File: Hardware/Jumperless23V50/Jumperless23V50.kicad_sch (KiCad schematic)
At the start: 218 parts, among them J1 Debug, J11 TopOutMAIN, J12 TopInMAIN, J13 BottomInMAIN, J14 5V, J15 BottomOutMAIN, J1711 Conn_01x15, J1712 Conn_01x15, J2 USB_C_Receptacle_USB2.0_16P, J3 ProbeJack, J4 Breadboard, J5 ProbeHeader, J6 CH446Q, J7 DaisyChain_OUT, J8 DaisyChain_IN, K1 CH446Q, Q3 Q_NPN_CBE, SW1 BOOT, SW3 RotaryEncoder_Switch, U1 LT1054, U10 L272D, U11 LM324, U1806 MCP4728, U1807 L272D, U2 NCP1117-3.3_SOT223, U3 INA219, U4 INA219, U5 RP2350_80QFN, U7 LM324, U8 W25Q128JVS, U9 RP2040, Y1 ABLS-12.000MHZ-B4-T

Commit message: Fixed lockups - added Apps to Menu - routed 23V50
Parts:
- removed C12: 1uF, Capacitor_SMD:C_0402_1005Metric, symbol JumperlessSymbols:C
- removed D63, D66: 1N4148, Diode_SMD:D_SOD-323, symbol JumperlessSymbols:1N4148W
- removed J5: ProbeHeader, JumperlessFootprints:probePads, symbol Connector_Generic:Conn_01x05
- removed R11, R83, R84, R9: 0R, Resistor_SMD:R_0402_1005Metric, symbol JumperlessSymbols:R_Small_US_2
- removed R2, R3: 22R, Resistor_SMD:R_0402_1005Metric, symbol JumperlessSymbols:R
- removed unit 4 of RN15
- removed unit 3 of RN15
- removed RN5: 0R, Resistor_SMD:R_Array_Convex_4x0402, symbol Device:R_Pack04_Split
- removed TP13: -8V, JumperlessFootprints:TestPoint_D0.75mm, symbol JumperlessSymbols:TestPoint
- removed TP14: +8V, JumperlessFootprints:TestPoint_D0.75mm, symbol JumperlessSymbols:TestPoint
- removed TP15: LED IN_FROM_WISHBONE, JumperlessFootprints:PINHEADER-1x1_vertical, symbol JumperlessSymbols:TestPoint
- removed TP2: TestPoint, JumperlessFootprints:TestPoint_Pad_D1.0mm, symbol Connector:TestPoint
- removed TP21: DAC_1, JumperlessFootprints:TestPoint_D0.75mm, symbol JumperlessSymbols:TestPoint
- removed U9: RP2040, JumperlessFootprints:RP2040-QFN-56, symbol JumperlessSymbols:RP2040
- added JP10: Nano GND Top - GPIO 24, JumperlessFootprints:SolderJumper-3_P1.3mm_Bridged12_Pad1.0x1.5mm, symbol JumperlessSymbols:SolderJumper_3_Bridged12
- added JP12: Nano GND Bot - GPIO 23, JumperlessFootprints:SolderJumper-3_P1.3mm_Bridged12_Pad1.0x1.5mm, symbol JumperlessSymbols:SolderJumper_3_Bridged12
- added JP13: GND, JumperlessFootprints:SolderJumper_2_Bridged_Small, symbol JumperlessSymbols:SolderJumper_2_Bridged
- added JP14: ADC, JumperlessFootprints:SolderJumper_2_Bridged_Small, symbol JumperlessSymbols:SolderJumper_2_Bridged
- added JP15: GP2, JumperlessFootprints:SolderJumper_2_Bridged_Small, symbol JumperlessSymbols:SolderJumper_2_Bridged
- added JP16: BUT, JumperlessFootprints:SolderJumper_2_Bridged_Small, symbol JumperlessSymbols:SolderJumper_2_Bridged
- added JP17: PRO, JumperlessFootprints:SolderJumper_2_Bridged_Small, symbol JumperlessSymbols:SolderJumper_2_Bridged
- added JP5: Reset 0 - Current Sense +, JumperlessFootprints:SolderJumper-3_P1.3mm_Bridged12_Pad1.0x1.5mm, symbol JumperlessSymbols:SolderJumper_3_Bridged12
- added JP6: Reset 1 - Current Sense -, JumperlessFootprints:SolderJumper-3_P1.3mm_Bridged12_Pad1.0x1.5mm, symbol JumperlessSymbols:SolderJumper_3_Bridged12
- added JP7: Reset 0, JumperlessFootprints:SolderJumper_2_Bridged_Small, symbol JumperlessSymbols:SolderJumper_2_Bridged
- added JP8: Reset 1, JumperlessFootprints:SolderJumper_2_Bridged_Small, symbol JumperlessSymbols:SolderJumper_2_Bridged
- added JP9: VIN - GPIO 25, JumperlessFootprints:SolderJumper-3_P1.3mm_Bridged12_Pad1.0x1.5mm, symbol JumperlessSymbols:SolderJumper_3_Bridged12
- added R2, R80, R89, R90: 0R, Resistor_SMD:R_0402_1005Metric_Pad0.72x0.64mm_HandSolder, symbol Device:R_Small_US
- added TP2: RUN, JumperlessFootprints:TestPoint_D0.75mm, symbol JumperlessSymbols:TestPoint
- added U12: ~, JumperlessFootprints:SolderJumper-Double, symbol JumperlessSymbols:SolderJumperDouble
- added U6: TLV73311PDBV, Package_TO_SOT_SMD:SOT-23-5, symbol Regulator_Linear:TLV73311PDBV
- added U9: LM2660MX, JumperlessFootprints:SOIC8, symbol Converter_DCDC:TC7662Bx0A
- A2, B1, C26, E1, F5, G1, H1, I1, K1, L1: LCSC (none) -> C109471; LCSC Part # (none) -> C109471
- C1, C4, C6: footprint Capacitor_SMD:C_1206_3216Metric_Pad1.33x1.80mm_HandSolder -> JumperlessFootprints:1210CAP; LCSC (none) -> C6120014
- C11, C9: value 1uF -> 10uF; footprint Capacitor_SMD:C_0402_1005Metric -> Capacitor_SMD:C_0603_1608Metric
- C16, C25: footprint RP2350_80QFN_minimal:C_0402_1005Metric_small_pads -> JumperlessFootprints:C_0402_1005Metric
- C2, C3, C5: value 10uF -> 22uF; footprint Capacitor_Tantalum_SMD:CP_EIA-3528-12_Kemet-T_Pad1.50x2.35mm_HandSolder -> JumperlessFootprints:1210CAP; LCSC C189401 -> C212712; LCSC Part # (none) -> C212712
- C27: value 0.1uF -> .1uF
- D61, D62, D65, D67, D68: footprint Diode_SMD:D_SOD-323 -> JumperlessFootprints:D_SOD-323; LCSC (none) -> C150183; LCSC Part # (none) -> C150183
- JP1: value NANO 3V3 -> NANO 3V3 - GPIO 27; footprint JumperlessFootprints:SolderJumper_2_Bridged_Small -> JumperlessFootprints:SolderJumper-3_P1.3mm_Bridged12_Pad1.0x1.5mm; symbol JumperlessSymbols:SolderJumper_2_Bridged -> JumperlessSymbols:SolderJumper_3_Bridged12; now left out of the parts list
- JP11: footprint Jumper:SolderJumper-3_P1.3mm_Bridged12_Pad1.0x1.5mm -> JumperlessFootprints:SolderJumper-3_P1.3mm_Bridged12_Pad1.0x1.5mm
- JP2: value NANO 5V -> NANO 5V - GPIO 26; footprint JumperlessFootprints:SolderJumper_2_Bridged_Small -> JumperlessFootprints:SolderJumper-3_P1.3mm_Bridged12_Pad1.0x1.5mm; symbol JumperlessSymbols:SolderJumper_2_Bridged -> JumperlessSymbols:SolderJumper_3_Bridged12; now left out of the parts list
- L2: LCSC (none) -> C2041573; LCSC Part # (none) -> C2041573
- Q3: value Q_NPN_CBE -> Q_NPN_BCE; footprint (none) -> Package_TO_SOT_SMD:SOT-23; symbol Device:Q_NPN_CBE -> Device:Q_NPN_BEC; LCSC (none) -> C909754; LCSC Part # (none) -> C909754
- R21, R55, R56, R58, R59, R60, R61, R62, R63, R64, R65, R66, R67, R68, R69, R70, R71, R72, R73, R74, R75, R76, R77, R78: LCSC C114765 -> C427231; LCSC Part # C114765 -> C427231
- R31: LCSC (none) -> C852887
- R6: LCSC (none) -> C852624; LCSC Part # (none) -> C852624
- R7, R88: LCSC (none) -> C131359; LCSC Part # (none) -> C131359
- R79: LCSC (none) -> C427231; LCSC Part # (none) -> C427231
- R8: value 47K -> 51100; LCSC (none) -> C852827; LCSC Part # (none) -> C852827
- R85, R86: LCSC C114765 -> C852651; LCSC Part # C114765 -> C852651
- RN10, RN19: LCSC C621323 -> C728748; LCSC Part # C621323 -> C728748
- RN12: value 10K -> 8.2K; LCSC C136853 -> C728757; LCSC Part # C136853 -> C728757
- RN13, RN16, RN7: value 6.8K -> 8.2K; LCSC C728919 -> C728757; LCSC Part # C728919 -> C728757
- RN14, RN17, RN6: LCSC C2769517 -> C620895; LCSC Part # C2769517 -> C620895
- RN15, RN18: LCSC C621323 -> C425315; LCSC Part # C621323 -> C425315
- RN15: renamed from RN11; LCSC C621323 -> C425315; LCSC Part # C621323 -> C425315
- RN18: renamed from RN15; LCSC C621323 -> C425315; LCSC Part # C621323 -> C425315
- RN2, RN3: LCSC (none) -> C425316; LCSC Part # (none) -> C425316
- RN4, RN8: LCSC C2769517 -> C2769517; LCSC Part # C2769517 -> C2769517
- SW1: LCSC (none) -> C22459525; LCSC Part # (none) -> C22459525
- SW3: LCSC (none) -> C29780879; LCSC Part # (none) -> C29780879
- TP22, TP23: footprint Symbol:BackMaskWindows -> JumperlessFootprints:backMaskWindowsNew
- TP5: value FB/SHDN -> +9V
- TP6: value VREF -> -9V
- U1: footprint JumperlessFootprints:DIP-8_W7.62mm -> JumperlessFootprints:DIP8; LCSC (none) -> C1355744; LCSC Part # (none) -> C1355744; now not fitted; now left out of the parts list
- U10, U1807: LCSC (none) -> C443843; LCSC Part # (none) -> C443843
- U11, U7: LCSC (none) -> C71035; LCSC Part # (none) -> C71035
- U1806: LCSC (none) -> C108207; LCSC Part # (none) -> C108207
- U2: LCSC (none) -> C22462596; LCSC Part # (none) -> C22462596
- U3, U4: footprint Package_SO:SOIC-8_3.9x4.9mm_P1.27mm -> JumperlessFootprints:SOIC8; LCSC (none) -> C138706; LCSC Part # (none) -> C138706
- U8: LCSC (none) -> C97521; LCSC Part # (none) -> C97521
- Y1: value ABLS-12.000MHZ-B4-T -> ABM8-272-T3; LCSC (none) -> C20625731; LCSC Part # (none) -> C20625731
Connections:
- net +1V1: now also R80.1, R89.2; no longer C11.1, C9.1, U5.65 (VREG_FB)
- net +5V: now also C11.1, C9.1, R2.1, U6.1 (IN), U6.3 (EN), U9.8 (V+)
- net +9V: now also TP5.1
- net -9V: now also TP6.1
- net 1: now also A2.35 (Y1); no longer K1.31 (X0)
- net 10: now also B1.39 (Y3); no longer B1.37 (Y2)
- net 11: now also B1.17 (Y4); no longer B1.39 (Y3)
- net 12: now also B1.15 (Y5); no longer B1.17 (Y4)
- net 13: now also B1.13 (Y6); no longer B1.15 (Y5)
- net 14: now also B1.11 (Y7); no longer B1.13 (Y6)
- net 15: now also C26.35 (Y1); no longer B1.11 (Y7)
- net 16: now also C26.37 (Y2); no longer C26.35 (Y1)
- net 17: now also C26.39 (Y3); no longer C26.37 (Y2)
- net 18: now also C26.17 (Y4); no longer C26.39 (Y3)
- net 19: now also C26.15 (Y5); no longer C26.17 (Y4)
- net 2: now also A2.37 (Y2); no longer A2.35 (Y1)
- net 20: now also C26.13 (Y6); no longer C26.15 (Y5)
- net 21: now also C26.11 (Y7); no longer C26.13 (Y6)
- net 22: now also D70.35 (Y1); no longer C26.11 (Y7)
- net 23: now also D70.37 (Y2); no longer D70.35 (Y1)
- net 24: now also D70.39 (Y3); no longer D70.37 (Y2)
- net 25: now also D70.17 (Y4); no longer D70.39 (Y3)
- net 26: now also D70.15 (Y5); no longer D70.17 (Y4)
- net 27: now also D70.13 (Y6); no longer D70.15 (Y5)
- net 28: now also D70.11 (Y7); no longer D70.13 (Y6)
- net 29: now also K1.31 (X0); no longer D70.11 (Y7)
- net 3: now also A2.39 (Y3); no longer A2.37 (Y2)
- net 30: now also L1.31 (X0); no longer K1.30 (X1)
- net 31: now also E1.35 (Y1); no longer L1.31 (X0)
- net 32: now also E1.37 (Y2); no longer E1.35 (Y1)
- net 33: now also E1.39 (Y3); no longer E1.37 (Y2)
- net 34: now also E1.17 (Y4); no longer E1.39 (Y3)
- net 35: now also E1.15 (Y5); no longer E1.17 (Y4)
- net 36: now also E1.13 (Y6); no longer E1.15 (Y5)
- net 37: now also E1.11 (Y7); no longer E1.13 (Y6)
- net 38: now also F5.35 (Y1); no longer E1.11 (Y7)
- net 39: now also F5.37 (Y2); no longer F5.35 (Y1)
- net 4: now also A2.17 (Y4); no longer A2.39 (Y3)
- net 40: now also F5.39 (Y3); no longer F5.37 (Y2)
- net 41: now also F5.17 (Y4); no longer F5.39 (Y3)
- net 42: now also F5.15 (Y5); no longer F5.17 (Y4)
- net 43: now also F5.13 (Y6); no longer F5.15 (Y5)
- net 44: now also F5.11 (Y7); no longer F5.13 (Y6)
- net 45: now also G1.35 (Y1); no longer F5.11 (Y7)
- net 46: now also G1.37 (Y2); no longer G1.35 (Y1)
- net 47: now also G1.39 (Y3); no longer G1.37 (Y2)
- net 48: now also G1.17 (Y4); no longer G1.39 (Y3)
- net 49: now also G1.15 (Y5); no longer G1.17 (Y4)
- net 5: now also A2.15 (Y5); no longer A2.17 (Y4)
- net 50: now also G1.13 (Y6); no longer G1.15 (Y5)
- net 51: now also G1.11 (Y7); no longer G1.13 (Y6)
- net 52: now also H1.35 (Y1); no longer G1.11 (Y7)
- net 53: now also H1.37 (Y2); no longer H1.35 (Y1)
- net 54: now also H1.39 (Y3); no longer H1.37 (Y2)
- net 55: now also H1.17 (Y4); no longer H1.39 (Y3)
- net 56: now also H1.15 (Y5); no longer H1.17 (Y4)
- net 57: now also H1.13 (Y6); no longer H1.15 (Y5)
- net 58: now also H1.11 (Y7); no longer H1.13 (Y6)
- net 59: now also K1.30 (X1); no longer H1.11 (Y7)
- net 6: now also A2.13 (Y6); no longer A2.15 (Y5)
- net 7: now also A2.11 (Y7); no longer A2.13 (Y6)
- net 8: now also B1.35 (Y1); no longer A2.11 (Y7)
- net 9: now also B1.37 (Y2); no longer B1.35 (Y1)
- net ADC_UNBUFFERED_+-8V_PROBE: now also JP14.1 (A); no longer J3.5 (R3)
- net CURR_SENSE+: now also JP5.1 (A), U12.4 (B); no longer I1.8 (X11)
- net CURR_SENSE-: now also JP6.1 (A), U12.5 (B); no longer J6.8 (X11)
- net DAC_1: now also U12.2 (A), U12.6 (C); no longer C10.1, RN8.5 (R4.2), TP8.1, U10.5
- net GND: now also JP10.1 (A), JP12.1 (A), JP13.1 (A), U6.2 (GND), U9.3 (GND); no longer A1.29 (GND), A1.4 (GND), J3.1 (S)
- net GPIO_2: now also JP15.1 (A); no longer J3.4 (R2)
- net GPIO_23: now also JP12.3 (B)
- net GPIO_24: now also JP10.3 (B)
- net GPIO_25: now also JP9.3 (B)
- net GPIO_26: now also JP2.3 (B)
- net GPIO_27: now also JP1.3 (B)
- net NANO_~{RESET}_0: now also JP5.3 (B), JP7.1 (A); no longer U5.18 (GPIO18)
- net NANO_~{RESET}_1: now also JP6.3 (B), JP8.1 (A); no longer U5.19 (GPIO19)
- net Probe_Button: now also JP16.1 (A); no longer J3.3 (R1)
- net Probe_Probe: now also JP17.1 (A); no longer J3.2 (T)
- net RUN: now also TP2.1
- net UART_Rx: now also U5.78 (GPIO1)
- net UART_Tx: now also U5.77 (GPIO0)
- net VIN: now also JP9.1 (A); no longer A1.30 (VIN)
- net VREG_LX: now also R90.2; no longer L2.2
- net Vout: now reaches C4.2, R7.1, U1.5 (-VOUT)
- net Vout: now also Q3.2 (E), U9.5 (VOUT); no longer Q3.3 (E)
- net at D65.1 (K), R7.2: now also Q3.3 (C); no longer Q3.1 (C)
- net at R6.1: now also Q3.1 (B); no longer Q3.2 (B)
- net VREF/LV: now reaches U1.6 (VREF)
- net VREF/LV: now also U9.6 (LV); no longer TP6.1
- net Cap+: now reaches C2.2, C3.1, U1.2 (CAP+)
- net Cap+: now also U9.2 (CAP+)
- net Cap-: now reaches C3.2, C5.1, U1.4 (CAP-)
- net Cap-: now also U9.4 (CAP-)
- net FP/Boost: now reaches U1.1 (FB/SHDN)
- net FP/Boost: now also R2.2, U9.1 (BOOST); no longer TP5.1
- net OSC: now reaches U1.7 (OSC)
- net OSC: now also U9.7 (OSC)
- new net: J3.1 (S), JP13.2 (B)
- new net: J3.2 (T), JP17.2 (B)
- new net: J3.3 (R1), JP16.2 (B)
- new net: J3.4 (R2), JP15.2 (B)
- new net: J3.5 (R3), JP14.2 (B)
- new net: A1.4 (GND), JP10.2 (C)
- new net: R89.1, U6.5 (OUT)
- new net: A1.30 (VIN), JP9.2 (C)
- new net: C10.1, RN8.5 (R4.2), TP8.1, U10.5, U12.3 (C)
- new net: A1.29 (GND), JP12.2 (C)
- new net: JP7.2 (B), U5.18 (GPIO18)
- new net: JP8.2 (B), U5.19 (GPIO19)
- new net: R80.2, U5.65 (VREG_FB)
- new net: J6.8 (X11), JP6.2 (C)
- new net: I1.8 (X11), JP5.2 (C)
- new net: L2.2, R90.1
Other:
- note added: "If we trade routable Nano Resets for Current Sense, we can cut these so they're +-9V tolerant"
- note added: "If you trade routable Nano Resets for Current Sensing, you can hook it up to read DAC 1 current to measure resistance (like DAC 0)"
- note added: "If you want to use a board with a completely different footprint, you can cut and swap all these solder jumpers so they're routable as GPIO 23-27"
- note added: "Rx and Tx relative to the RP2350"
- note added: "So I can swap over to the LDO if this SMPS is being a dick"
- note added: "This is just to make it easy to swap things if I fuck something up"
- note added: "This is to help it not fail startup when Vout goes above any other pin (weird)"
- note removed: "Drop supply voltage by 1 or 2 diode drops so crosspoints don't see voltages too near their supply voltage"
- note removed: "Rx and Tx are relative to the RP2040"
- note removed: "Try the LDO too"
- moved on the sheet: A2, B1, C1, C2, C26, C3, C4, C5, C6, D61, D62, D65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

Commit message: add updates
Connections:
- net +5V: no longer U1.8 (V+)
- net Cap+: no longer U1.2 (CAP+)
- net Cap-: no longer U1.4 (CAP-)
- net FP/Boost: no longer U1.1 (FB/SHDN)
- net GND: no longer U1.3 (GND)
- net OSC: no longer U1.7 (OSC)
- net VREF/LV: no longer U1.6 (VREF)
- net Vout: no longer U1.5 (-VOUT)
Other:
- moved on the sheet: C1, C11, C2, C3, C4, C5, C6, C9, D61, D62, D65, D67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

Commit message: Add FPC breakout and almost finished V5r4
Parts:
- removed D61: 1N5819, JumperlessFootprints:D_SOD-323, symbol JumperlessSymbols:1N5819
- removed Q3: Q_NPN_BCE, Package_TO_SOT_SMD:SOT-23, symbol Device:Q_NPN_BEC
- removed R2, R7: 0R, Resistor_SMD:R_0402_1005Metric_Pad0.72x0.64mm_HandSolder, symbol Device:R_Small_US
- removed R6: 1K, Resistor_SMD:R_0402_1005Metric_Pad0.72x0.64mm_HandSolder, symbol Device:R_Small_US
- removed RN2, RN3: 0R, Resistor_SMD:R_Array_Convex_4x0402, symbol Device:R_Pack04_Split
- added D2, D3: 1N5819, JumperlessFootprints:D_SOD-323, symbol JumperlessSymbols:1N5819
- added D4, D6, D7: 1N4148, JumperlessFootprints:D_SOD-323, symbol JumperlessSymbols:1N5819
- added J5: FPC Connector, JumperlessFootprints:FPC FC05-S20FCT, symbol Connector:Conn_01x20_Socket
- added JP18: 3V BP, JumperlessFootprints:SolderJumper_2_Bridged_Small, symbol Jumper:SolderJumper_2_Open
- added JP19: 5V BP, JumperlessFootprints:SolderJumper_2_Bridged_Small, symbol JumperlessSymbols:SolderJumper_2_Bridged
- added JP20: SolderJumper_3_Bridged12, JumperlessFootprints:SolderJumper-3_P1.3mm_Bridged12_Pad1.0x1.5mm, symbol Jumper:SolderJumper_3_Bridged12
- added JP21, JP22: 0, JumperlessFootprints:R_0603_1608Metric, symbol Device:R_Small_US
- added JP23: GPIO_0, JumperlessFootprints:SolderJumper_2_Bridged_Small, symbol Jumper:SolderJumper_2_Bridged
- added JP24: GPIO_1, JumperlessFootprints:SolderJumper_2_Bridged_Small, symbol Jumper:SolderJumper_2_Bridged
- added JP25: GPIO_2, JumperlessFootprints:SolderJumper_2_Bridged_Small, symbol Jumper:SolderJumper_2_Bridged
- added JP26: GPIO_3, JumperlessFootprints:SolderJumper_2_Bridged_Small, symbol Jumper:SolderJumper_2_Bridged
- added JP27: GPIO_4, JumperlessFootprints:SolderJumper_2_Bridged_Small, symbol Jumper:SolderJumper_2_Bridged
- added JP28: GPIO_5, JumperlessFootprints:SolderJumper_2_Bridged_Small, symbol Jumper:SolderJumper_2_Bridged
- added JP29: GPIO_6, JumperlessFootprints:SolderJumper_2_Bridged_Small, symbol Jumper:SolderJumper_2_Bridged
- added JP30: GPIO_7, JumperlessFootprints:SolderJumper_2_Bridged_Small, symbol Jumper:SolderJumper_2_Bridged
- added JP31: Boost, JumperlessFootprints:SolderJumper_2_Bridged_Small, symbol JumperlessSymbols:SolderJumper_2_Bridged
- added R3: 51100, Resistor_SMD:R_0402_1005Metric, symbol JumperlessSymbols:R_Small_US_2
- added TP10: VIN, JumperlessFootprints:TestPoint_D0.75mm, symbol JumperlessSymbols:TestPoint
- D67: value 1N5819 -> 1N4148; LCSC C150183 -> (none); LCSC Part # C150183 -> (none)
- JP1: symbol JumperlessSymbols:SolderJumper_3_Bridged12 -> Jumper:SolderJumper_3_Open
- R21, R55, R56, R58, R59, R60, R61, R62, R63, R64, R65, R66, R67, R68, R69, R70, R71, R72, R73, R74, R75, R76, R77, R78: value 33 -> 220; LCSC C427231 -> C25091; LCSC Part # C427231 -> C25091
- TP2: value RUN -> TestPoint
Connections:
- net +3V3: now also D2.2 (A), JP18.2 (B), R3.1; no longer JP1.1 (A)
- net +5V: now also U1.8 (V+), D3.2 (A), J5.1 (Pin_1), JP19.2 (B), JP31.2 (B); no longer JP2.1 (A)
- net +9V: now also D7.1 (K), JP22.1; no longer C1.1
- net -9V: now also D4.2 (A), JP21.2; no longer C6.2, D67.2 (A)
- net ADC_UNBUFFERED_+-8V_0: now also J5.15 (Pin_15)
- net ADC_UNBUFFERED_+-8V_1: now also J5.16 (Pin_16)
- net ADC_UNBUFFERED_+-8V_2: now also J5.17 (Pin_17)
- net ADC_UNBUFFERED_+-8V_3: now also J5.18 (Pin_18)
- net Cap+: now also U1.2 (CAP+)
- net Cap-: now also U1.4 (CAP-)
- net DAC_0: now also J5.19 (Pin_19)
- net DAC_1: now also J5.20 (Pin_20)
- net FP/Boost: now also U1.1 (FB/SHDN), JP31.1 (A)
- net GND: now also U1.3 (GND), J5.2 (Pin_2)
- net GPIO_2: no longer J7.11 (Pin_11), J8.11 (Pin_11)
- net GPIO_20: now also J5.3 (Pin_3), JP23.2 (B)
- net GPIO_21: now also J5.4 (Pin_4), JP24.2 (B)
- net GPIO_22: now also J5.5 (Pin_5), JP25.2 (B)
- net GPIO_23: now also J5.6 (Pin_6), JP26.2 (B)
- net GPIO_24: now also J5.7 (Pin_7), JP27.2 (B)
- net GPIO_25: now also J5.8 (Pin_8), JP28.2 (B)
- net GPIO_26: now also J5.9 (Pin_9), JP29.2 (B)
- net GPIO_27: now also J5.10 (Pin_10), JP30.2 (B)
- net GPIO_3: now also JP20.2 (C); no longer J7.12 (Pin_12), J8.12 (Pin_12)
- net GPIO_6: now also J5.13 (Pin_13)
- net GPIO_7: now also J5.14 (Pin_14)
- net OSC: now also U1.7 (OSC)
- net RESET: now also R3.2
- net RUN: no longer TP2.1
- net UART_Rx: now also J7.12 (Pin_12), J8.12 (Pin_12), J5.12 (Pin_12)
- net UART_Tx: now also J7.11 (Pin_11), J8.11 (Pin_11), J5.11 (Pin_11)
- net VIN: now also TP10.1
- net VREF/LV: now also U1.6 (VREF)
- net Vout: now also D65.1 (K), U1.5 (-VOUT)
- net RP_GPIO_27: now reaches U5.28 (GPIO27)
- net RP_GPIO_27: now also JP30.1 (A)
- net at C2.1, D62.1 (K): now also D6.2 (A)
- net RP_GPIO_25: now reaches U5.26 (GPIO25)
- net RP_GPIO_25: now also JP28.1 (A)
- net RP_GPIO_20: now reaches U5.20 (GPIO20)
- net RP_GPIO_20: now also JP23.1 (A)
- net RP_GPIO_21: now reaches U5.21 (GPIO21)
- net RP_GPIO_21: now also JP24.1 (A)
- net RP_GPIO_22: now reaches U5.22 (GPIO22)
- net RP_GPIO_22: now also JP25.1 (A)
- net RP_GPIO_23: now reaches U5.23 (GPIO23)
- net RP_GPIO_23: now also JP26.1 (A)
- net RP_GPIO_24: now reaches U5.25 (GPIO24)
- net RP_GPIO_24: now also JP27.1 (A)
- net RP_GPIO_26: now reaches U5.27 (GPIO26)
- net RP_GPIO_26: now also JP29.1 (A)
- new net: D2.1 (K), JP1.1 (A), JP18.1 (A)
- new net: C1.1, D6.1 (K), D7.2 (A), JP22.2
- new net: D3.1 (K), JP19.1 (A), JP2.1 (A)
- new net: C6.2, D4.1 (K), D67.2 (A), JP21.1
- new net LED_60_OUT: JP20.3 (B), TP2.1
- new net LED_RAILS_IN: JP20.1 (A)
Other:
- note added: "220"
- note added: "Another diode drop to get down from +-10V -> +-9V"
- note added: "Cut these to disconnect GPIO from RP2350 so daisy chain lines are 9V tolerant"
- note added: "FPC Connector 20-pin 0.5mm pitch for Bus Pirate and Daisy Chaining"
- note added: "Footprint for old LT1054 charge pump (just in case)"
- note added: "Probe"
- note added: "We're splitting the WS2812 data lines into 2 separate chains, so Rails, Nano Header, and Logo are driven separately from BB (for better frame rates)"
- note removed: "This is to help it not fail startup when Vout goes above any other pin (weird)"
- moved on the sheet: C27, J3, J7, JP13, JP14, JP15, JP16, JP17, JP7, JP8, R21, R22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

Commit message: routed V5r4
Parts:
- C2, C3, C5: value 22uF -> 10uF; LCSC C212712 -> C2918502; LCSC Part # C212712 -> C2918502
- J5: LCSC Part # (none) -> C2998828
- L2: LCSC C2041573 -> C41347751; LCSC Part # C2041573 -> C41347751
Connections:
- net GND: now also U9.6 (LV)
- net VREF/LV: no longer U9.6 (LV)
- net GPIO_2 renamed LED_OUT_PROBE
- net GPIO_3 renamed LED_OUT_TOP
- new net EncoderMP: SW3.0 (MP)

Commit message: pre-production revision
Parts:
- JP21, JP22: now not fitted
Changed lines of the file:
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@@
 		(in_bom yes)
 		(on_board yes)
-		(dnp no)
+		(dnp yes)
 		(property "Reference" "JP22"
 			(at 515.366 77.47 0)
@@
 		(in_bom yes)
 		(on_board yes)
-		(dnp no)
+		(dnp yes)
 		(property "Reference" "JP21"
 			(at 606.298 119.38 0)

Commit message: Rev 4 hardware
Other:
- note added: "Footprint for old LT1054 charge pump (just in case the LM2660MX betrays me)"
- note removed: "Footprint for old LT1054 charge pump (just in case)"
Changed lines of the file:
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@@
 	)
 	(junction
-		(at 594.995 90.17)
-		(diameter 0)
-		(color 0 0 0 0)
-	)
-	(junction
 		(at 505.46 77.47)
 		(diameter 0)
@@
 	)
 	(junction
-		(at 561.34 99.06)
-		(diameter 0)
-		(color 0 0 0 0)
-	)
-	(junction
 		(at 557.53 278.13)
 		(diameter 0)
@@
 	)
 	(junction
+		(at 565.785 123.19)
+		(diameter 0)
+		(color 0 0 0 0)
+	)
+	(junction
 		(at 351.79 251.46)
 		(diameter 0)
@@
 	)
 	(junction
-		(at 575.945 121.92)
-		(diameter 0)
-		(color 0 0 0 0)
-	)
-	(junction
 		(at 351.79 173.99)
 		(diameter 0)
@@
 	)
 	(junction
-		(at 565.785 121.92)
-		(diameter 0)
-		(color 0 0 0 0)
-	)
-	(junction
 		(at 344.17 438.15)
 		(diameter 0)
@@
 	)
 	(junction
+		(at 589.28 90.17)
+		(diameter 0)
+		(color 0 0 0 0)
+	)
+	(junction
 		(at 175.26 193.04)
 		(diameter 0)
@@
 	(wire
 		(pts
-			(xy 539.75 89.535) (xy 539.75 99.06)
-		)
-		(stroke
-			(width 0)
-			(type default)
-		)
-	)
-	(wire
-		(pts
 			(xy 73.025 436.245) (xy 73.025 438.15)
 		)
@@
 	(wire
 		(pts
+			(xy 565.785 123.19) (xy 571.5 123.19)
+		)
+		(stroke
+			(width 0)
+			(type default)
+		)
+	)
+	(wire
+		(pts
 			(xy 69.85 304.8) (xy 81.28 304.8)
 		)
@@
 	(wire
 		(pts
-			(xy 565.785 121.92) (xy 575.945 121.92)
+			(xy 166.37 440.69) (xy 166.37 443.23)
 		)
 		(stroke
@@
 	(wire
 		(pts
-			(xy 166.37 440.69) (xy 166.37 443.23)
+			(xy 227.33 181.61) (xy 227.33 182.88)
 		)
 		(stroke
@@
 	(wire
 		(pts
-			(xy 227.33 181.61) (xy 227.33 182.88)
+			(xy 575.945 121.92) (xy 571.5 121.92)
 		)
 		(stroke
@@
 	(wire
 		(pts
-			(xy 594.995 89.535) (xy 594.995 90.17)
+			(xy 589.28 89.535) (xy 589.28 90.17)
 		)
 		(stroke
@@
 	(wire
 		(pts
-			(xy 594.995 89.535) (xy 539.75 89.535)
-		)
-		(stroke
-			(width 0)
-			(type default)
-		)
-	)
-	(wire
-		(pts
-			(xy 539.75 99.06) (xy 541.02 99.06)
+			(xy 589.28 89.535) (xy 541.02 89.535)
 		)
 		(stroke
@@
 	(wire
 		(pts
+			(xy 589.28 90.17) (xy 589.28 107.95)
+		)
+		(stroke
+			(width 0)
+			(type default)
+		)
+	)
+	(wire
+		(pts
 			(xy 351.79 164.465) (xy 351.79 166.37)
 		)
@@
 	(wire
 		(pts
-			(xy 589.28 90.17) (xy 589.28 107.95)
-		)
-		(stroke
-			(width 0)
-			(type default)
-		)
-	)
-	(wire
-		(pts
 			(xy 651.51 471.17) (xy 671.83 471.17)
 		)
@@
 	(wire
 		(pts
+			(xy 180.34 367.03) (xy 180.34 364.49)
+		)
+		(stroke
+			(width 0)
+			(type default)
+		)
+	)
+	(wire
+		(pts
 			(xy 529.59 111.76) (xy 528.955 111.76)
 		)
@@
 	(wire
 		(pts
-			(xy 561.34 99.06) (xy 562.61 99.06)
-		)
-		(stroke
-			(width 0)
-			(type default)
-		)
-	)
-	(wire
-		(pts
 			(xy 107.95 270.51) (xy 107.95 273.685)
 		)
@@
 	(wire
 		(pts
+			(xy 571.5 121.92) (xy 571.5 123.19)
+		)
+		(stroke
+			(width 0)
+			(type default)
+		)
+	)
+	(wire
+		(pts
 			(xy 688.975 193.04) (xy 688.975 190.5)
 		)
@@
 		)
 	)
+	(wire
+		(pts
+			(xy 541.02 89.535) (xy 541.02 99.06)
+		)
+		(stroke
+			(width 0)
+			(type default)
+		)
+	)
 	(bus
 		(pts
@@
 	(rectangle
 		(start 154.94 332.74)
-		(end 219.075 367.665)
+		(end 219.075 370.84)
 		(stroke
 			(width 0)
@@
 		)
 	)
-	(text "Footprint for old\nLT1054 charge pump\n(just in case)"
+	(text "Footprint for old\nLT1054 charge pump\n(just in case the \nLM2660MX betrays me)"
 		(exclude_from_sim no)
-		(at 497.84 119.634 0)
+		(at 497.84 117.602 0)
 		(effects
 			(font
@@
 	(global_label "EncoderMP"
 		(shape input)
-		(at 180.34 364.49 270)
+		(at 180.34 367.03 0)
 		(fields_autoplaced yes)
 		(effects
@@
 				(size 1.27 1.27)
 			)
-			(justify right)
+			(justify left)
 		)
 		(property "Intersheetrefs" "${INTERSHEET_REFS}"
-			(at 180.34 377.756 90)
+			(at 193.606 367.03 0)
 			(effects
 				(font
 					(size 1.27 1.27)
 				)
-				(justify right)
+				(justify left)
 				(hide yes)
 			)
@@
 	(global_label "Vout"
 		(shape input)
-		(at 539.75 93.98 0)
+		(at 541.02 91.44 180)
 		(fields_autoplaced yes)
 		(effects
@@
 				(size 1.27 1.27)
 			)
-			(justify left)
+			(justify right)
 		)
 		(property "Intersheetrefs" "${INTERSHEET_REFS}"
-			(at 546.8475 93.98 0)
+			(at 533.9225 91.44 0)
 			(effects
 				(font
 					(size 1.27 1.27)
 				)
-				(justify left)
+				(justify right)
 				(hide yes)
 			)
@@
 		(on_board yes)
 		(dnp no)
-		(fields_autoplaced yes)
 		(property "Reference" "U9"
 			(at 553.3741 91.44 0)
@@
 		)
 		(property "Value" "LM2660MX"
-			(at 553.3741 93.98 0)
+			(at 548.386 94.488 0)
 			(effects
 				(font
@@
 		)
 		(property "Value" "1N5819"
-			(at 566.547 128.27 90)
+			(at 570.484 126.238 90)
 			(effects
 				(font
@@
 		(dnp no)
 		(property "Reference" "TP5"
-			(at 503.809 71.628 0)
+			(at 507.238 71.882 0)
 			(effects
 				(font
@@
 		)
 		(property "Value" "+9V"
-			(at 503.555 72.898 0)
+			(at 506.73 73.914 0)
 			(effects
 				(font
@@
 		)
 		(property "Value" "1N4148"
-			(at 579.755 119.38 0)
+			(at 581.914 118.872 0)
 			(effects
 				(font

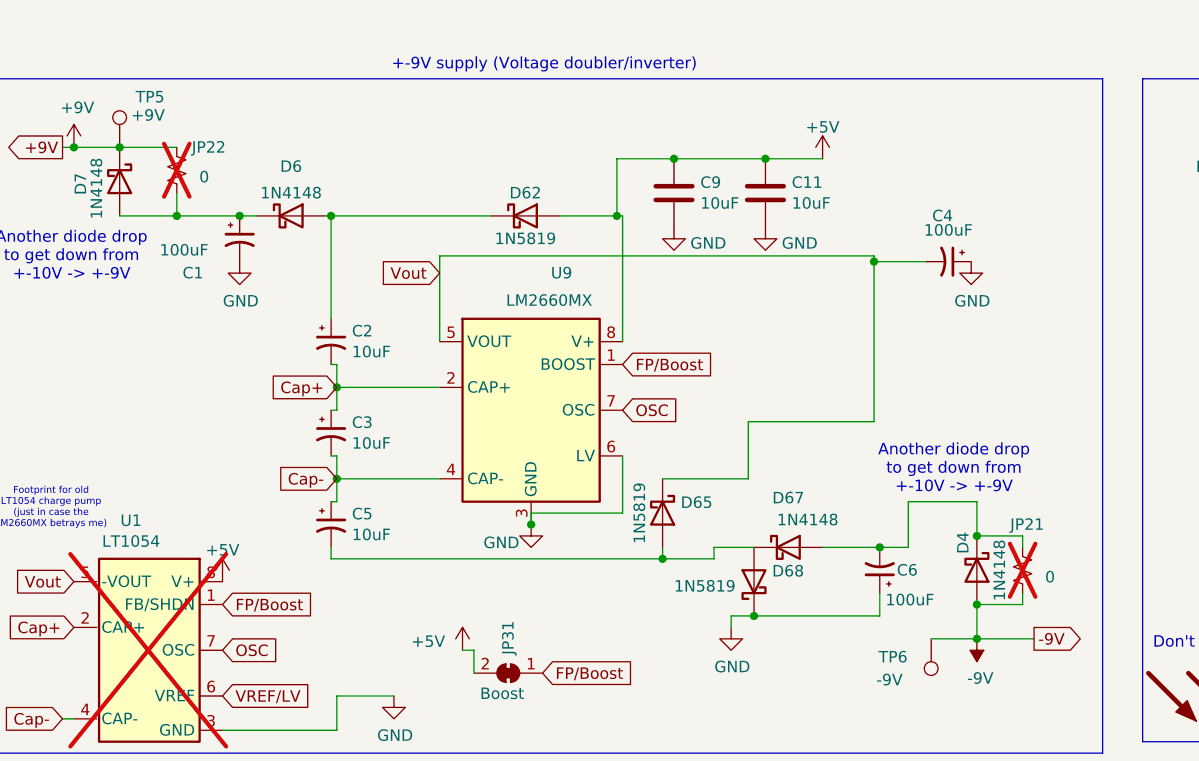
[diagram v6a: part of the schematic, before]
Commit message: Cleaned/sped up probe current measurement, fixed the inability to switch to slot 0 (duh), screwed around with my ghetto mutex
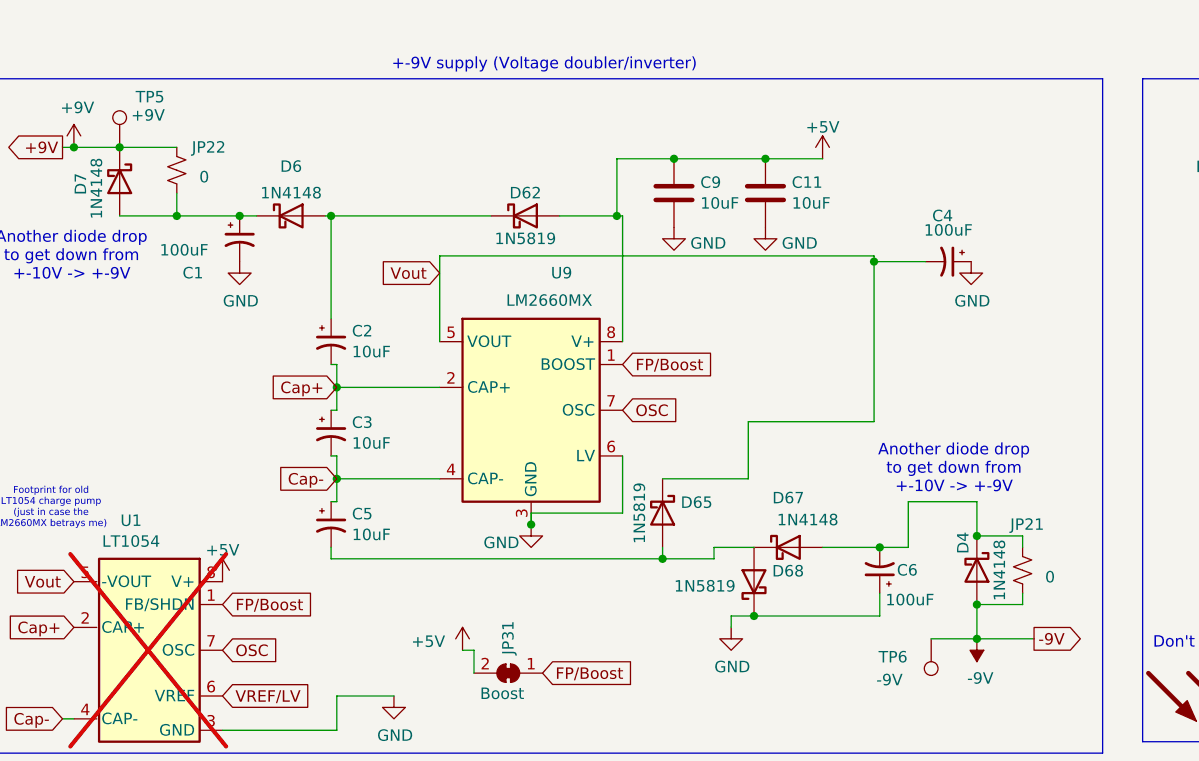
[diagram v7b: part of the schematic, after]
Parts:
- JP21, JP22: now fitted
